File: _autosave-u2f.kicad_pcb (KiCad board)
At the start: 2 copper layers, 8 parts, among them P1 Touch Button, P2 V33prog, P3 D- prog, P4 USB_A, U1 ch552T

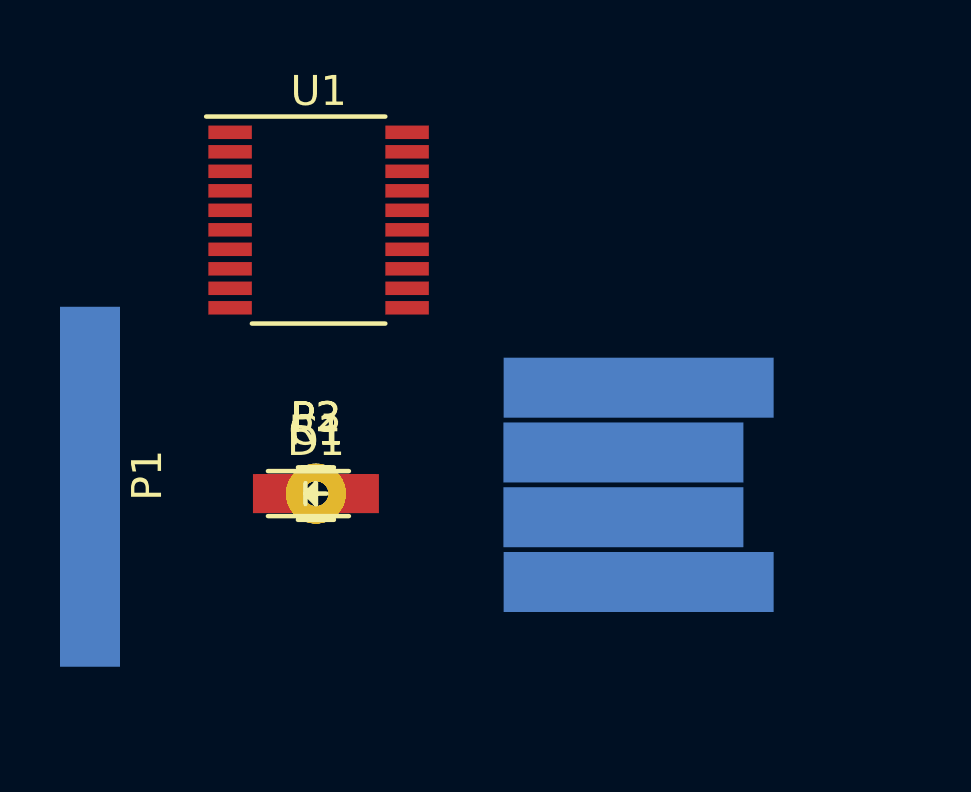
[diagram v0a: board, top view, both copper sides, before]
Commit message: added some new footprints and stuff.
I'm having issues connecting everything up while keeping my optimal dimensions.
Options are to
- switch around some the GPIO pins (for LED) to avoid having traces run accross components
- Remove resistor and offload it to only when I'm programming (or directly wire D- and VCC to a "resistor", which will only be there during programmin)
- Remove programming pins and pre-program chip before putting it on the board (then I'd have to design a programmer PCB)
- (nucelar option) add an extra layer (basically two because I've never heard of a 3-layer PCB)
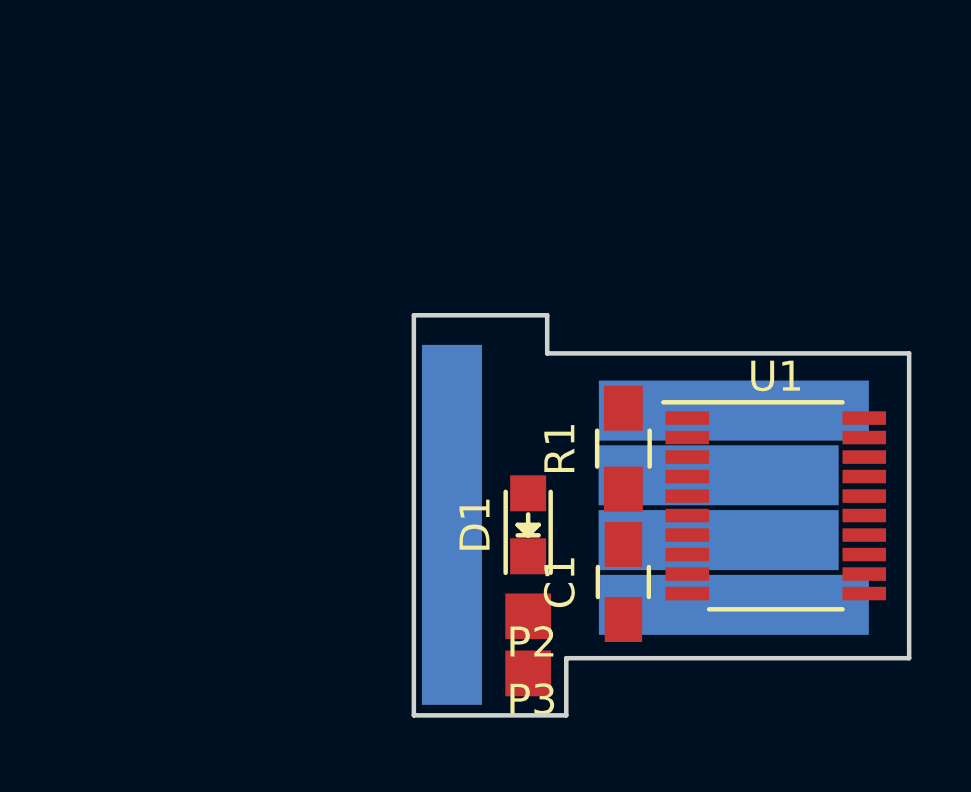
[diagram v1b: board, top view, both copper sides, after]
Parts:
- P1, P4: moved to B.Cu
- P2, P3: footprint Wire_Pads:SolderWirePad_single_0-8mmDrill -> u2f:tp
- moved U1 18.0 mm to (163.8, 105.4)
- moved P1 12.1 mm to (153.0, 106.0), turned to 270 degrees
- moved C1 10.7 mm to (158.8, 108.0), turned to 90 degrees
- moved R1 10.4 mm to (158.8, 103.5), turned to 90 degrees
- moved P3 9.35 mm to (155.6, 111.1)
- moved P2 8.24 mm to (155.6, 109.2)
- moved D1 7.15 mm to (155.6, 106.0), turned to 90 degrees
- moved P4 3.24 mm to (161.9, 105.4)
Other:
- board outline added: 16.5 x 13.3 mm
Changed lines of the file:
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@@
     (links 12)
     (no_connects 12)
-    (area 0 0 0 0)
+    (area 137.963 90.61 163.958 111.049)
     (thickness 1.6)
-    (drawings 0)
+    (drawings 8)
     (tracks 0)
     (zones 0)
@@
   (layers
     (0 F.Cu signal)
-    (31 B.Cu signal hide)
+    (31 B.Cu signal)
     (32 B.Adhes user)
     (33 F.Adhes user)
@@
     (pad_to_mask_clearance 0.2)
     (aux_axis_origin 0 0)
-    (visible_elements FFFFFF7F)
+    (visible_elements FFFFFB1F)
     (pcbplotparams
       (layerselection 0x00030_80000001)
@@
   )
   (module Capacitors_SMD:C_0805_HandSoldering (layer F.Cu)
-    (at 148.5011 105.0036)
+    (at 158.75 107.95 90)
     (descr "Capacitor SMD 0805, hand soldering")
     (tags "capacitor 0805")
     (attr smd)
-    (fp_text reference C1 (at 0 -2.1) (layer F.SilkS)
-      (effects (font (size 1 1) (thickness 0.15)))
-    )
-    (fp_text value C (at 0 2.1) (layer F.Fab)
+    (fp_text reference C1 (at 0 -2.1 90) (layer F.SilkS)
+      (effects (font (size 1 1) (thickness 0.15)))
+    )
+    (fp_text value C (at 0 2.1 90) (layer F.Fab)
       (effects (font (size 1 1) (thickness 0.15)))
     )
@@
     (fp_line (start 0.5 -0.85) (end -0.5 -0.85) (layer F.SilkS) (width 0.15))
     (fp_line (start -0.5 0.85) (end 0.5 0.85) (layer F.SilkS) (width 0.15))
-    (pad 1 smd rect (at -1.25 0) (size 1.5 1.25) (layers F.Cu F.Paste F.Mask)
+    (pad 1 smd rect (at -1.25 0 90) (size 1.5 1.25) (layers F.Cu F.Paste F.Mask)
       (net 1 +5V))
-    (pad 2 smd rect (at 1.25 0) (size 1.5 1.25) (layers F.Cu F.Paste F.Mask)
+    (pad 2 smd rect (at 1.25 0 90) (size 1.5 1.25) (layers F.Cu F.Paste F.Mask)
       (net 2 GND))
     (model Capacitors_SMD.3dshapes/C_0805_HandSoldering.wrl
@@
   )
   (module LEDs:LED_0805 (layer F.Cu)
-    (at 148.5011 105.0036)
+    (at 155.575 106.045 90)
     (descr "LED 0805 smd package")
     (tags "LED 0805 SMD")
     (attr smd)
-    (fp_text reference D1 (at 0 -1.75) (layer F.SilkS)
-      (effects (font (size 1 1) (thickness 0.15)))
-    )
-    (fp_text value LED (at 0 1.75) (layer F.Fab)
+    (fp_text reference D1 (at 0 -1.75 90) (layer F.SilkS)
+      (effects (font (size 1 1) (thickness 0.15)))
+    )
+    (fp_text value LED (at 0 1.75 90) (layer F.Fab)
       (effects (font (size 1 1) (thickness 0.15)))
     )
@@
     (fp_line (start -1.9 0.95) (end -1.9 -0.95) (layer F.CrtYd) (width 0.05))
     (fp_line (start -1.9 -0.95) (end 1.9 -0.95) (layer F.CrtYd) (width 0.05))
-    (pad 2 smd rect (at 1.04902 0 180) (size 1.19888 1.19888) (layers F.Cu F.Paste F.Mask)
+    (pad 2 smd rect (at 1.04902 0 270) (size 1.19888 1.19888) (layers F.Cu F.Paste F.Mask)
       (net 3 "Net-(D1-Pad2)"))
-    (pad 1 smd rect (at -1.04902 0 180) (size 1.19888 1.19888) (layers F.Cu F.Paste F.Mask)
+    (pad 1 smd rect (at -1.04902 0 270) (size 1.19888 1.19888) (layers F.Cu F.Paste F.Mask)
       (net 2 GND))
     (model LEDs.3dshapes/LED_0805.wrl
@@
     )
   )
-  (module u2f:EdgeTouch (layer F.Cu)
-    (at 140.97 104.775 90)
-    (fp_text reference P1 (at 0.381 1.905 90) (layer F.SilkS)
-      (effects (font (size 1 1) (thickness 0.15)))
-    )
-    (fp_text value "Touch Button" (at 0 -2.032 90) (layer F.Fab)
-      (effects (font (size 1 1) (thickness 0.15)))
-    )
-    (pad 1 connect rect (at 0 0 90) (size 12 2) (layers B.Cu F.Mask)
+  (module u2f:EdgeTouch (layer B.Cu)
+    (at 153.035 106.045 270)
+    (fp_text reference P1 (at 0.381 -1.905 270) (layer B.SilkS)
+      (effects (font (size 1 1) (thickness 0.15)) (justify mirror))
+    )
+    (fp_text value "Touch Button" (at 0 2.032 270) (layer B.Fab)
+      (effects (font (size 1 1) (thickness 0.15)) (justify mirror))
+    )
+    (pad 1 connect rect (at 0 0 270) (size 12 2) (layers B.Cu B.Mask)
       (net 4 "Net-(P1-Pad1)"))
   )
-  (module Wire_Pads:SolderWirePad_single_0-8mmDrill (layer F.Cu)
-    (at 148.5011 105.0036)
-    (fp_text reference P2 (at 0 -2.54) (layer F.SilkS)
-      (effects (font (size 1 1) (thickness 0.15)))
-    )
-    (fp_text value V33prog (at 0 2.54) (layer F.Fab)
-      (effects (font (size 1 1) (thickness 0.15)))
-    )
-    (pad 1 thru_hole circle (at 0 0) (size 1.99898 1.99898) (drill 0.8001) (layers *.Cu *.Mask)
+  (module u2f:tp (layer F.Cu)
+    (at 155.575 109.22)
+    (fp_text reference P2 (at 0.127 0.754) (layer F.SilkS)
+      (effects (font (size 1 1) (thickness 0.15)))
+    )
+    (fp_text value V33prog (at 0.127 -0.246) (layer F.Fab)
+      (effects (font (size 1 1) (thickness 0.15)))
+    )
+    (pad 1 connect rect (at 0 -0.127) (size 1.524 1.524) (layers F.Cu F.Mask)
       (net 5 "Net-(P2-Pad1)"))
   )
-  (module Wire_Pads:SolderWirePad_single_0-8mmDrill (layer F.Cu)
-    (at 148.5011 105.0036)
-    (fp_text reference P3 (at 0 -2.54) (layer F.SilkS)
-      (effects (font (size 1 1) (thickness 0.15)))
-    )
-    (fp_text value "D- prog" (at 0 2.54) (layer F.Fab)
-      (effects (font (size 1 1) (thickness 0.15)))
-    )
-    (pad 1 thru_hole circle (at 0 0) (size 1.99898 1.99898) (drill 0.8001) (layers *.Cu *.Mask)
+  (module u2f:tp (layer F.Cu)
+    (at 155.575 111.125)
+    (fp_text reference P3 (at 0.127 0.754) (layer F.SilkS)
+      (effects (font (size 1 1) (thickness 0.15)))
+    )
+    (fp_text value "D- prog" (at 0.127 -0.246) (layer F.Fab)
+      (effects (font (size 1 1) (thickness 0.15)))
+    )
+    (pad 1 connect rect (at 0 -0.127) (size 1.524 1.524) (layers F.Cu F.Mask)
       (net 6 "Net-(P3-Pad1)"))
   )
-  (module u2f:USBEdge (layer F.Cu)
-    (at 158.75 104.775)
-    (fp_text reference P4 (at -0.762 5.199) (layer B.SilkS)
+  (module u2f:USBEdge (layer B.Cu)
+    (at 161.925 105.41)
+    (fp_text reference P4 (at -0.762 -5.199) (layer B.SilkS)
       (effects (font (size 1 1) (thickness 0.15)) (justify mirror))
     )
-    (fp_text value USB_A (at 0 -5.58) (layer B.Fab)
+    (fp_text value USB_A (at 0 5.58) (layer B.Fab)
       (effects (font (size 1 1) (thickness 0.15)) (justify mirror))
     )
-    (pad 3 connect rect (at 0 1.016) (size 8 2) (layers B.Cu F.Mask)
+    (pad 3 connect rect (at 0 -1.016) (size 8 2) (layers B.Cu B.Mask)
       (net 7 "Net-(P4-Pad3)"))
-    (pad 2 connect rect (at 0 -1.143) (size 8 2) (layers B.Cu F.Mask)
+    (pad 2 connect rect (at 0 1.143) (size 8 2) (layers B.Cu B.Mask)
       (net 8 "Net-(P4-Pad2)"))
-    (pad 1 connect rect (at 0.508 -3.302) (size 9 2) (layers B.Cu F.Mask)
+    (pad 1 connect rect (at 0.508 3.302) (size 9 2) (layers B.Cu B.Mask)
       (net 1 +5V))
-    (pad 4 connect rect (at 0.508 3.175) (size 9 2) (layers B.Cu F.Mask)
+    (pad 4 connect rect (at 0.508 -3.175) (size 9 2) (layers B.Cu B.Mask)
       (net 2 GND))
-    (pad 5 connect rect (at -3.429 3.048) (size 1 1) (layers B.Cu F.Mask)
+    (pad 5 connect rect (at -3.429 -3.048) (size 1 1) (layers B.Cu B.Mask)
       (net 22 "Net-(P4-Pad5)"))
   )
   (module Resistors_SMD:R_0805_HandSoldering (layer F.Cu)
-    (at 148.5011 105.0036)
+    (at 158.75 103.505 90)
     (descr "Resistor SMD 0805, hand soldering")
     (tags "resistor 0805")
     (attr smd)
-    (fp_text reference R1 (at 0 -2.1) (layer F.SilkS)
-      (effects (font (size 1 1) (thickness 0.15)))
-    )
-    (fp_text value R (at 0 2.1) (layer F.Fab)
+    (fp_text reference R1 (at 0 -2.1 90) (layer F.SilkS)
+      (effects (font (size 1 1) (thickness 0.15)))
+    )
+    (fp_text value R (at 0 2.1 90) (layer F.Fab)
       (effects (font (size 1 1) (thickness 0.15)))
     )
@@
     (fp_line (start 0.6 0.875) (end -0.6 0.875) (layer F.SilkS) (width 0.15))
     (fp_line (start -0.6 -0.875) (end 0.6 -0.875) (layer F.SilkS) (width 0.15))
-    (pad 1 smd rect (at -1.35 0) (size 1.5 1.3) (layers F.Cu F.Paste F.Mask)
+    (pad 1 smd rect (at -1.35 0 90) (size 1.5 1.3) (layers F.Cu F.Paste F.Mask)
       (net 6 "Net-(P3-Pad1)"))
-    (pad 2 smd rect (at 1.35 0) (size 1.5 1.3) (layers F.Cu F.Paste F.Mask)
+    (pad 2 smd rect (at 1.35 0 90) (size 1.5 1.3) (layers F.Cu F.Paste F.Mask)
       (net 8 "Net-(P4-Pad2)"))
     (model Resistors_SMD.3dshapes/R_0805_HandSoldering.wrl
@@
   )
   (module Housings_SSOP:TSSOP-20_4.4x6.5mm_Pitch0.65mm (layer F.Cu)
-    (at 148.59 95.885)
+    (at 163.83 105.41)
     (descr "20-Lead Plastic Thin Shrink Small Outline (ST)-4.4 mm Body [TSSOP] (see Microchip Packaging Specification 00000049BS.pdf)")
     (tags "SSOP 0.65")
@@
     )
   )
+  (gr_line (start 156.845 110.49) (end 168.275 110.49) (angle 90) (layer Edge.Cuts) (width 0.15))
+  (gr_line (start 156.845 112.395) (end 156.845 110.49) (angle 90) (layer Edge.Cuts) (width 0.15))
+  (gr_line (start 151.765 112.395) (end 156.845 112.395) (angle 90) (layer Edge.Cuts) (width 0.15))
+  (gr_line (start 151.765 99.06) (end 151.765 112.395) (angle 90) (layer Edge.Cuts) (width 0.15))
+  (gr_line (start 156.21 99.06) (end 151.765 99.06) (angle 90) (layer Edge.Cuts) (width 0.15))
+  (gr_line (start 156.21 100.33) (end 156.21 99.06) (angle 90) (layer Edge.Cuts) (width 0.15))
+  (gr_line (start 168.275 100.33) (end 156.21 100.33) (angle 90) (layer Edge.Cuts) (width 0.15))
+  (gr_line (start 168.275 110.49) (end 168.275 100.33) (angle 90) (layer Edge.Cuts) (width 0.15))
 )
